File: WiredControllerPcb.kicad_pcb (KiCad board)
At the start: 2 copper layers, 90 x 50 mm, 37 parts, among them J1 Joystick, J2 Conn_01x06, J3 Conn_01x04, J4 Conn_01x06, SW1 SW_Push, SW2 SW_Push, SW3 SW_Push, SW4 SW_Push, U1 LP2985-3.3, U2 ATmega328P-MU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

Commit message: Update pcb design for revision 2019.09
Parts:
- removed C5, C6: 12pf, Capacitor_SMD:C_0402_1005Metric
- removed Y1: 8MHz, Crystal:Crystal_SMD_SeikoEpson_FA238-4Pin_3.2x2.5mm
- added J5: Conn_01x04, Connector_PinHeader_2.54mm:PinHeader_1x04_P2.54mm_Vertical, F.Cu at (141.1, 61.3)
- added JP2: Jumper_NO, Jumper:SolderJumper-2_P1.3mm_Open_RoundedPad1.0x1.5mm, F.Cu at (153.1, 53.0)
- added JP3: Jumper_NO, Jumper:SolderJumper-2_P1.3mm_Open_RoundedPad1.0x1.5mm, F.Cu at (155.4, 53.0)
- added R7: 1k, Resistor_SMD:R_0603_1608Metric, F.Cu at (153.1, 58.5)
- added R8: 1k, Resistor_SMD:R_0603_1608Metric, F.Cu at (154.6, 58.5)
- J2: footprint Connector_PinHeader_2.00mm:PinHeader_2x03_P2.00mm_Vertical_SMD -> footprints:2x03_P2.54mm_Pads
- J4: value Conn_01x06 -> Conn_01x04; footprint Connector_PinHeader_2.00mm:PinHeader_2x03_P2.00mm_Vertical_SMD -> TerminalBlock:TerminalBlock_bornier-4_P5.08mm; moved to F.Cu
- JP1: value Jumper_NC_Small -> Jumper_NO
- moved J4 43.3 mm to (120.9, 54.0), turned to 0 degrees
- moved JP1 5.25 mm to (158.8, 53.0), turned to 270 degrees
- moved C1 4.34 mm to (133.5, 60.6)
- moved C2 4.34 mm to (130.3, 60.7)
- moved C3 4.34 mm to (129.8, 63.4)
- moved U1 4.34 mm to (132.7, 63.4)
- moved R5 1.06 mm to (120.6, 63.0)
- moved D1 0.19 mm to (136.4, 64.2)
- moved D2 0.19 mm to (141.7, 64.2)
- moved D3 0.19 mm to (146.8, 64.2)
- moved D4 0.19 mm to (151.8, 64.2)
- moved R1 0.19 mm to (138.1, 64.2)
- moved R2 0.19 mm to (143.4, 64.2)
- moved R3 0.19 mm to (148.3, 64.2)
- moved R4 0.19 mm to (153.3, 64.2)
- renumbered R6 to R4, R4 to R5, R5 to R6
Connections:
- C1 pad 1: VCC -> VDC
- J2 pad 1: /MOSI -> /MISO
- J2 pad 2: VCC -> VDC
- J2 pad 4: /MISO -> /MOSI
- J3 pad 3: VCC -> VDC
- J4 pad 1: /RST -> /SCL
- J4 pad 2: /0RX -> /SDA
- J4 pad 3: /1TX -> VDC
- J4 pad 4: VCC -> GND
- R4 pad 1: /LED3 -> /LED4
- U1 pad 1: VCC -> VDC
- U1 pad 3: VCC -> VDC
- U2 pad 19: /LED3 -> Net-(U2-Pad19)
- U2 pad 22: /LED4 -> Net-(U2-Pad22)
- U2 pad 30: /0RX -> /LED3
- U2 pad 31: /1TX -> /LED4
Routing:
- net VDC: track 0.00 -> 79.2 mm
- net VCC: track 79.0 -> 0.00 mm
- net /SCL: track 27.4 -> 99.4 mm, vias 1 -> 0
- net /SDA: track 26.5 -> 91.1 mm, vias 1 -> 0
- net /LED4: track 0.00 -> 27.1 mm, vias 0 -> 2
- net /BTNT: track 64.0 -> 89.1 mm, vias 1 -> 0
- net GND: track 252.1 -> 228.2 mm
- net +3V3: track 56.3 -> 76.9 mm
- net /0RX: track 17.7 -> 0.00 mm, vias 1 -> 0
- net /1TX: track 17.1 -> 0.00 mm, vias 1 -> 0
- net /SCK: track 22.0 -> 33.9 mm
- net Net-(U2-Pad8): track 7.15 -> 0.00 mm
- net /RST: track 41.0 -> 36.3 mm
- net Net-(JP3-Pad2): track 0.00 -> 4.41 mm
- net Net-(JP2-Pad2): track 0.00 -> 4.09 mm
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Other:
- board text added: "Jumper to change address."
- board text added: "Pull up I2C"
- board text added: "Rev2019.09"
- board text added: "SCL"
- board text added: "SDA"
- board text added: "VDC"
- board text removed: "RX"
- board text removed: "Rev2019.08"
- board text removed: "TX"
- board text removed: "VCC"

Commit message: Change resister to pullup to 10k from 1k
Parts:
- R7, R8: value 1k -> 10k
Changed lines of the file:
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@@
       (effects (font (size 1 1) (thickness 0.15)))
     )
-    (fp_text value 1k (at 0 1.43 90) (layer F.Fab)
+    (fp_text value 10k (at 0 1.43 90) (layer F.Fab)
       (effects (font (size 1 1) (thickness 0.15)))
     )
@@
       (effects (font (size 1 1) (thickness 0.15)))
     )
-    (fp_text value 1k (at 0 1.43 90) (layer F.Fab)
+    (fp_text value 10k (at 0 1.43 90) (layer F.Fab)
       (effects (font (size 1 1) (thickness 0.15)))
     )

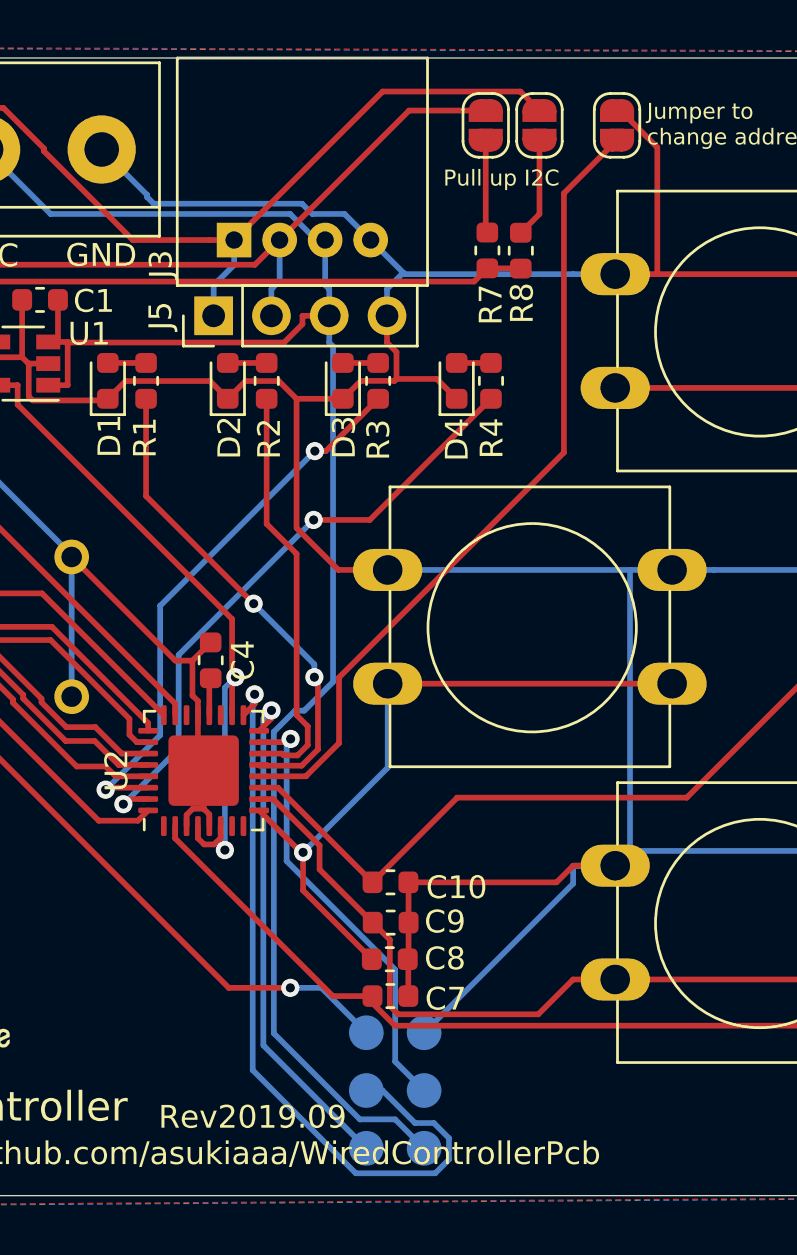
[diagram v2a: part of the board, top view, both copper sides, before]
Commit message: Correct connection ADDR and GND
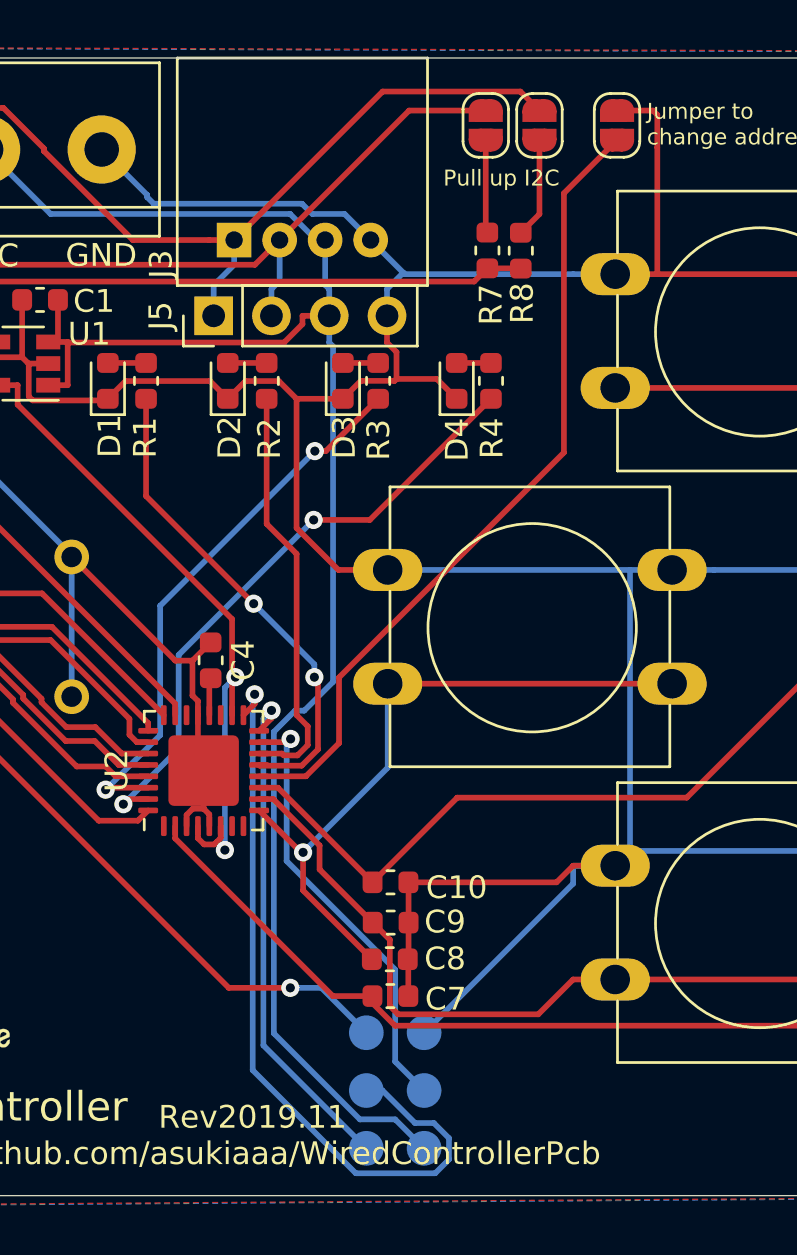
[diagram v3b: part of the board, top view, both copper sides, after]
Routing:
- net GND: track 228.2 -> 229.2 mm
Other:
- board text added: "Rev2019.11"
- board text removed: "Rev2019.09"
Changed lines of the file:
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@@
     (thickness 1.6)
     (drawings 31)
-    (tracks 371)
+    (tracks 373)
     (zones 0)
     (modules 39)
@@
     (effects (font (size 1 1) (thickness 0.15)))
   )
-  (gr_text Rev2019.09 (at 142.81 96.55) (layer F.SilkS)
+  (gr_text Rev2019.11 (at 142.81 96.55) (layer F.SilkS)
     (effects (font (size 1 1) (thickness 0.15)))
   )
@@
   (segment (start 158.75 59.5) (end 160.5993 59.5) (width 0.25) (layer F.Cu) (net 1))
   (segment (start 160.5993 59.5) (end 160.5993 53.9291) (width 0.25) (layer F.Cu) (net 1))
-  (segment (start 160.5993 53.9291) (end 158.9802 52.31) (width 0.25) (layer F.Cu) (net 1))
   (segment (start 158.9802 52.31) (end 158.83 52.31) (width 0.25) (layer F.Cu) (net 1))
   (segment (start 159.4007 84.8493) (end 158.75 85.5) (width 0.25) (layer B.Cu) (net 1))
@@
   (segment (start 140.1819 82.9944) (end 140.66 82.9944) (width 0.25) (layer F.Cu) (net 1))
   (segment (start 140.66 82.9944) (end 140.66 81.32) (width 0.25) (layer F.Cu) (net 1))
+  (segment (start 158.83 52.31) (end 160.41 52.31) (width 0.25) (layer F.Cu) (net 1))
+  (segment (start 160.5993 52.4993) (end 160.5993 53.9291) (width 0.25) (layer F.Cu) (net 1))
+  (segment (start 160.41 52.31) (end 160.5993 52.4993) (width 0.25) (layer F.Cu) (net 1))
   (segment (start 131.63 62.48) (end 130.7747 62.48) (width 0.25) (layer F.Cu) (net 2))
   (segment (start 130.7747 62.48) (end 130.7747 60.9828) (width 0.25) (layer F.Cu) (net 2))

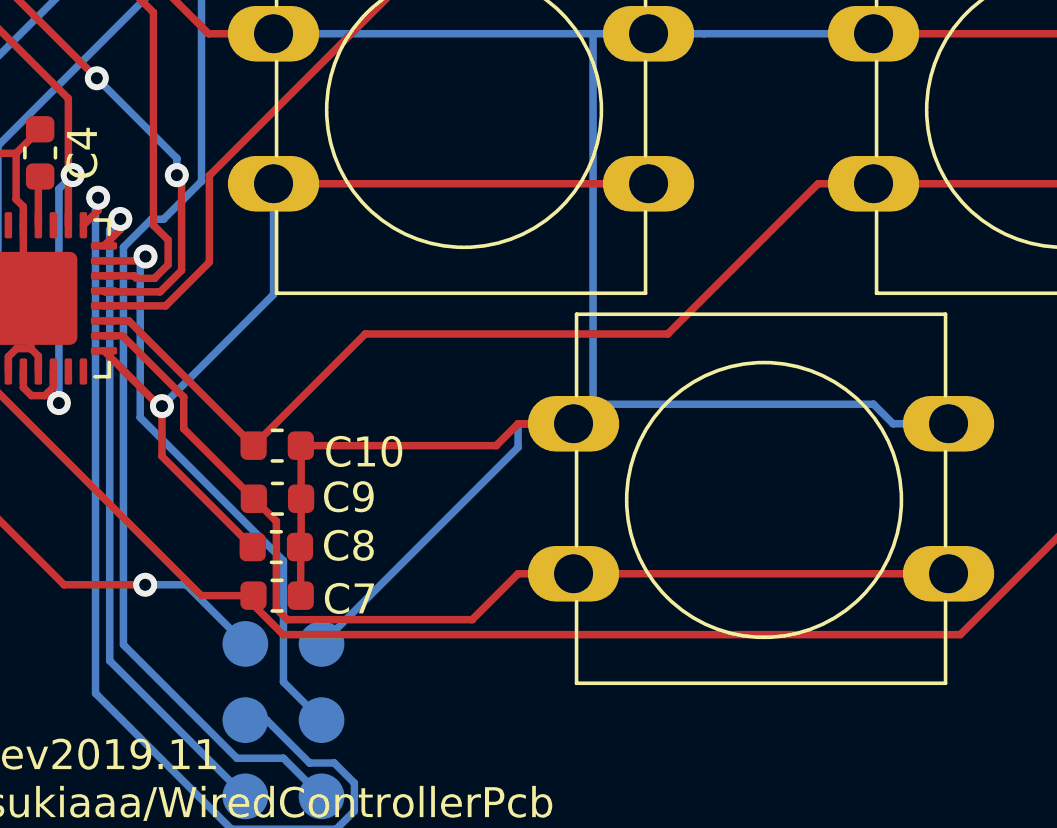
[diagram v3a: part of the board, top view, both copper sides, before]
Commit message: Correct position of right button and bottom button
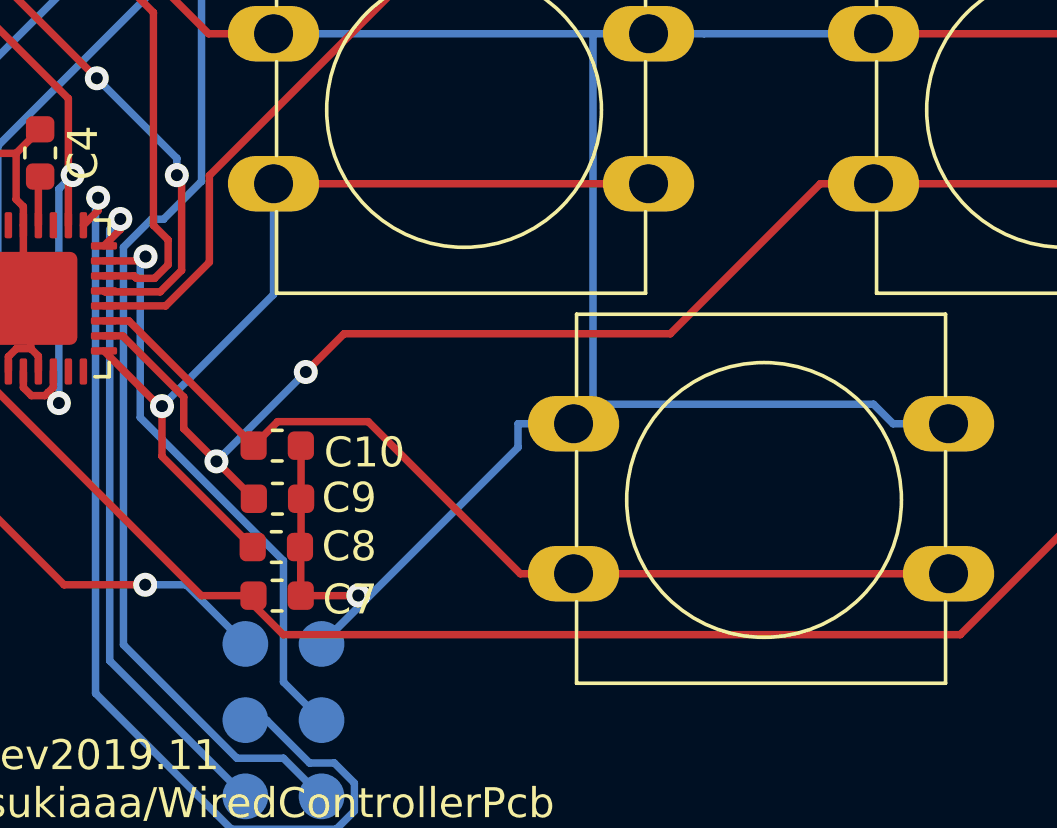
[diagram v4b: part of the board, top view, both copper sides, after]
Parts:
- moved SW3 16.4 mm to (175.0, 75.0)
- moved SW4 16.4 mm to (165.0, 88.0)
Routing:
- net /BTNB: track 43.5 -> 32.3 mm
- net /BTNR: track 35.0 -> 46.1 mm, vias 0 -> 2
- net GND: track 229.2 -> 223.8 mm, vias 0 -> 1
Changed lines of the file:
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@@
     (thickness 1.6)
     (drawings 31)
-    (tracks 373)
+    (tracks 377)
     (zones 0)
     (modules 39)
@@
   )
   (module footprints:SW_Center_PUSH-12mm (layer F.Cu)
-    (at 175 75)
+    (at 165 88)
     (descr "SW PUSH 12mm https://www.e-switch.com/system/asset/product_line/data_sheet/143/TL1100.pdf")
     (tags "tact sw push 12mm")
@@
   )
   (module footprints:SW_Center_PUSH-12mm (layer F.Cu)
-    (at 165 88)
+    (at 175 75)
     (descr "SW PUSH 12mm https://www.e-switch.com/system/asset/product_line/data_sheet/143/TL1100.pdf")
     (tags "tact sw push 12mm")
@@
   (segment (start 161.25 72.5) (end 159.4007 72.5) (width 0.25) (layer B.Cu) (net 1))
   (segment (start 149.6675 86.23) (end 149.6595 86.23) (width 0.25) (layer F.Cu) (net 1))
-  (segment (start 156.9007 85.5) (end 156.1707 86.23) (width 0.25) (layer F.Cu) (net 1))
-  (segment (start 156.1707 86.23) (end 149.6675 86.23) (width 0.25) (layer F.Cu) (net 1))
   (segment (start 149.6675 86.23) (end 149.6675 88) (width 0.25) (layer F.Cu) (net 1))
   (segment (start 116 72.46) (end 121.08 72.46) (width 0.25) (layer B.Cu) (net 1))
@@
   (segment (start 149.6555 89.636) (end 149.6295 89.61) (width 0.25) (layer F.Cu) (net 1))
   (segment (start 181.25 72.5) (end 168.75 72.5) (width 0.25) (layer F.Cu) (net 1))
-  (segment (start 158.75 85.5) (end 156.9007 85.5) (width 0.25) (layer F.Cu) (net 1))
   (segment (start 148.72 61.33) (end 148.72 62.5053) (width 0.25) (layer F.Cu) (net 1))
   (segment (start 140.66 82.9944) (end 140.91 83.2444) (width 0.25) (layer F.Cu) (net 1))
@@
   (segment (start 160.5993 52.4993) (end 160.5993 53.9291) (width 0.25) (layer F.Cu) (net 1))
   (segment (start 160.41 52.31) (end 160.5993 52.4993) (width 0.25) (layer F.Cu) (net 1))
+  (segment (start 149.6555 91.23) (end 151.57 91.23) (width 0.25) (layer F.Cu) (net 1))
+  (via (at 151.575 91.225) (size 0.8) (drill 0.4) (layers F.Cu B.Cu) (net 1))
+  (segment (start 151.57 91.23) (end 151.575 91.225) (width 0.25) (layer F.Cu) (net 1))
+  (segment (start 151.575 91.615) (end 150.35 92.84) (width 0.25) (layer B.Cu) (net 1))
+  (segment (start 151.575 91.225) (end 151.575 91.615) (width 0.25) (layer B.Cu) (net 1))
   (segment (start 131.63 62.48) (end 130.7747 62.48) (width 0.25) (layer F.Cu) (net 2))
   (segment (start 130.7747 62.48) (end 130.7747 60.9828) (width 0.25) (layer F.Cu) (net 2))
@@
   (segment (start 161.25 77.5) (end 148.75 77.5) (width 0.25) (layer F.Cu) (net 22))
   (via (at 145.0312 84.9125) (size 0.8) (layers F.Cu B.Cu) (net 22))
-  (segment (start 158.75 90.5) (end 156.9007 90.5) (width 0.25) (layer F.Cu) (net 23))
-  (segment (start 148.0925 88) (end 148.8442 88.7517) (width 0.25) (layer F.Cu) (net 23))
-  (segment (start 148.8442 88.7517) (end 148.8442 91.6658) (width 0.25) (layer F.Cu) (net 23))
-  (segment (start 148.8442 91.6658) (end 149.2096 92.0312) (width 0.25) (layer F.Cu) (net 23))
-  (segment (start 149.2096 92.0312) (end 155.3695 92.0312) (width 0.25) (layer F.Cu) (net 23))
-  (segment (start 155.3695 92.0312) (end 156.9007 90.5) (width 0.25) (layer F.Cu) (net 23))
   (segment (start 143.0975 82.57) (end 143.7172 82.57) (width 0.25) (layer F.Cu) (net 23))
   (segment (start 143.7172 82.57) (end 145.7565 84.6093) (width 0.25) (layer F.Cu) (net 23))
   (segment (start 145.7565 84.6093) (end 145.7565 85.664) (width 0.25) (layer F.Cu) (net 23))
-  (segment (start 145.7565 85.664) (end 148.0925 88) (width 0.25) (layer F.Cu) (net 23))
-  (segment (start 171.25 90.5) (end 158.75 90.5) (width 0.25) (layer F.Cu) (net 23))
+  (via (at 146.84625 86.75375) (size 0.8) (drill 0.4) (layers F.Cu B.Cu) (net 23))
+  (segment (start 146.84625 86.75375) (end 148.0925 88) (width 0.25) (layer F.Cu) (net 23))
+  (segment (start 145.7565 85.664) (end 146.84625 86.75375) (width 0.25) (layer F.Cu) (net 23))
+  (via (at 149.825 83.775) (size 0.8) (drill 0.4) (layers F.Cu B.Cu) (net 23))
+  (segment (start 146.84625 86.75375) (end 149.825 83.775) (width 0.25) (layer B.Cu) (net 23))
+  (segment (start 149.825 83.775) (end 151.1 82.5) (width 0.25) (layer F.Cu) (net 23))
+  (segment (start 161.976 82.5) (end 151.1 82.5) (width 0.25) (layer F.Cu) (net 23))
+  (segment (start 166.976 77.5) (end 161.976 82.5) (width 0.25) (layer F.Cu) (net 23))
+  (segment (start 168.75 77.5) (end 166.976 77.5) (width 0.25) (layer F.Cu) (net 23))
+  (segment (start 181.25 77.5) (end 168.75 77.5) (width 0.25) (layer F.Cu) (net 23))
+  (segment (start 171.25 90.5) (end 158.75 90.5) (width 0.25) (layer F.Cu) (net 24))
   (segment (start 148.0845 86.23) (end 143.9245 82.07) (width 0.25) (layer F.Cu) (net 24))
   (segment (start 143.9245 82.07) (end 143.0975 82.07) (width 0.25) (layer F.Cu) (net 24))
-  (segment (start 148.0845 86.23) (end 151.8066 82.5079) (width 0.25) (layer F.Cu) (net 24))
-  (segment (start 151.8066 82.5079) (end 161.8928 82.5079) (width 0.25) (layer F.Cu) (net 24))
-  (segment (start 161.8928 82.5079) (end 166.9007 77.5) (width 0.25) (layer F.Cu) (net 24))
-  (segment (start 168.75 77.5) (end 166.9007 77.5) (width 0.25) (layer F.Cu) (net 24))
-  (segment (start 181.25 77.5) (end 168.75 77.5) (width 0.25) (layer F.Cu) (net 24))
+  (segment (start 156.976 90.5) (end 158.75 90.5) (width 0.25) (layer F.Cu) (net 24))
+  (segment (start 151.90599 85.42999) (end 156.976 90.5) (width 0.25) (layer F.Cu) (net 24))
+  (segment (start 148.88451 85.42999) (end 151.90599 85.42999) (width 0.25) (layer F.Cu) (net 24))
+  (segment (start 148.0845 86.23) (end 148.88451 85.42999) (width 0.25) (layer F.Cu) (net 24))
   (segment (start 151.78 63.4025) (end 153.29 63.4025) (width 0.25) (layer F.Cu) (net 26))
   (segment (start 143.0975 81.57) (end 145.1544 81.57) (width 0.25) (layer F.Cu) (net 27))

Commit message: Add pull up resistor to reset pin
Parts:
- added R9: 10k, Resistor_SMD:R_0603_1608Metric, F.Cu at (138.0, 86.2)
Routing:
- net +3V3: track 76.9 -> 80.4 mm, vias 2 -> 3
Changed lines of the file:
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@@
-(kicad_pcb (version 20171130) (host pcbnew 5.1.4-e60b266~84~ubuntu18.04.1)
+(kicad_pcb (version 20171130) (host pcbnew 5.1.5-52549c5~84~ubuntu18.04.1)
   (general
     (thickness 1.6)
     (drawings 31)
-    (tracks 377)
+    (tracks 382)
     (zones 0)
-    (modules 39)
+    (modules 40)
     (nets 37)
   )
@@
     (add_net "Net-(U2-Pad8)")
     (add_net VDC)
+  )
+  (module Resistor_SMD:R_0603_1608Metric (layer F.Cu)
+    (at 137.9625 86.2 180)
+    (descr "Resistor SMD 0603 (1608 Metric), square (rectangular) end terminal, IPC_7351 nominal, (Body size source: http://www.tortai-tech.com/upload/download/2011102023233369053.pdf), generated with kicad-footprint-generator")
+    (tags resistor)
+    (attr smd)
+    (fp_text reference R9 (at 0 -1.43) (layer F.SilkS)
+      (effects (font (size 1 1) (thickness 0.15)))
+    )
+    (fp_text value 10k (at 0 1.43) (layer F.Fab)
+      (effects (font (size 1 1) (thickness 0.15)))
+    )
+    (fp_text user %R (at 0 0) (layer F.Fab)
+      (effects (font (size 0.4 0.4) (thickness 0.06)))
+    )
+    (fp_line (start 1.48 0.73) (end -1.48 0.73) (layer F.CrtYd) (width 0.05))
+    (fp_line (start 1.48 -0.73) (end 1.48 0.73) (layer F.CrtYd) (width 0.05))
+    (fp_line (start -1.48 -0.73) (end 1.48 -0.73) (layer F.CrtYd) (width 0.05))
+    (fp_line (start -1.48 0.73) (end -1.48 -0.73) (layer F.CrtYd) (width 0.05))
+    (fp_line (start -0.162779 0.51) (end 0.162779 0.51) (layer F.SilkS) (width 0.12))
+    (fp_line (start -0.162779 -0.51) (end 0.162779 -0.51) (layer F.SilkS) (width 0.12))
+    (fp_line (start 0.8 0.4) (end -0.8 0.4) (layer F.Fab) (width 0.1))
+    (fp_line (start 0.8 -0.4) (end 0.8 0.4) (layer F.Fab) (width 0.1))
+    (fp_line (start -0.8 -0.4) (end 0.8 -0.4) (layer F.Fab) (width 0.1))
+    (fp_line (start -0.8 0.4) (end -0.8 -0.4) (layer F.Fab) (width 0.1))
+    (pad 2 smd roundrect (at 0.7875 0 180) (size 0.875 0.95) (layers F.Cu F.Paste F.Mask) (roundrect_rratio 0.25)
+      (net 12 /RST))
+    (pad 1 smd roundrect (at -0.7875 0 180) (size 0.875 0.95) (layers F.Cu F.Paste F.Mask) (roundrect_rratio 0.25)
+      (net 3 +3V3))
+    (model ${KISYS3DMOD}/Resistor_SMD.3dshapes/R_0603_1608Metric.wrl
+      (at (xyz 0 0 0))
+      (scale (xyz 1 1 1))
+      (rotate (xyz 0 0 0))
+    )
   )
   (module Connector_PinHeader_2.54mm:PinHeader_1x04_P2.54mm_Vertical (layer F.Cu)
@@
   (via (at 141.5945 84.8109) (size 0.8) (layers F.Cu B.Cu) (net 3))
   (via (at 142.0545 77.2115) (size 0.8) (layers F.Cu B.Cu) (net 3))
+  (via (at 139.925 86.275) (size 0.8) (drill 0.4) (layers F.Cu B.Cu) (net 3))
+  (segment (start 141.5945 84.8109) (end 141.3891 84.8109) (width 0.25) (layer B.Cu) (net 3))
+  (segment (start 141.3891 84.8109) (end 139.925 86.275) (width 0.25) (layer B.Cu) (net 3))
+  (segment (start 138.825 86.275) (end 138.75 86.2) (width 0.25) (layer F.Cu) (net 3))
+  (segment (start 139.925 86.275) (end 138.825 86.275) (width 0.25) (layer F.Cu) (net 3))
   (segment (start 140.91 78.8825) (end 140.91 77.32) (width 0.25) (layer F.Cu) (net 4))
   (segment (start 140.91 77.32) (end 140.97 77.26) (width 0.25) (layer F.Cu) (net 4))
